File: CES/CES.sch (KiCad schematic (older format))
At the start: 4 parts, among them J101 Barrel_Jack

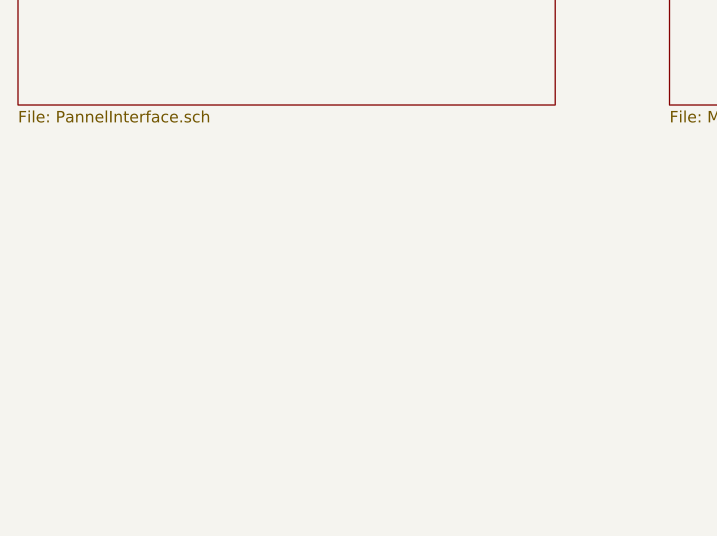
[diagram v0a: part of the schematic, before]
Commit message: Address decoding. Clock. Pannel buttons
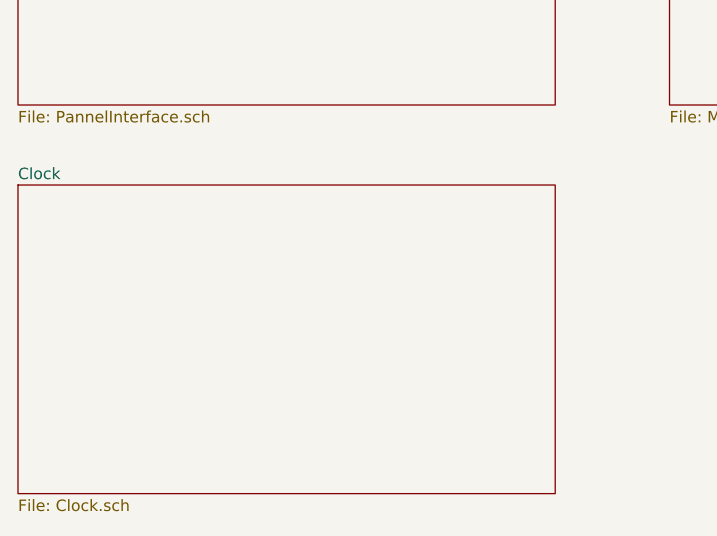
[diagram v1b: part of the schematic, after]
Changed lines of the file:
@@
 $Descr A4 11693 8268
 encoding utf-8
-Sheet 1 13
+Sheet 1 15
 Title "CES"
 Date "2021-04-24"
@@
 	10750 2200 10750 2150
 Connection ~ 10350 2200
+$Sheet
+S 1200 6000 2350 1350
+U 611BF25E
+F0 "Clock" 50
+F1 "Clock.sch" 50
+$EndSheet
 $EndSCHEMATC

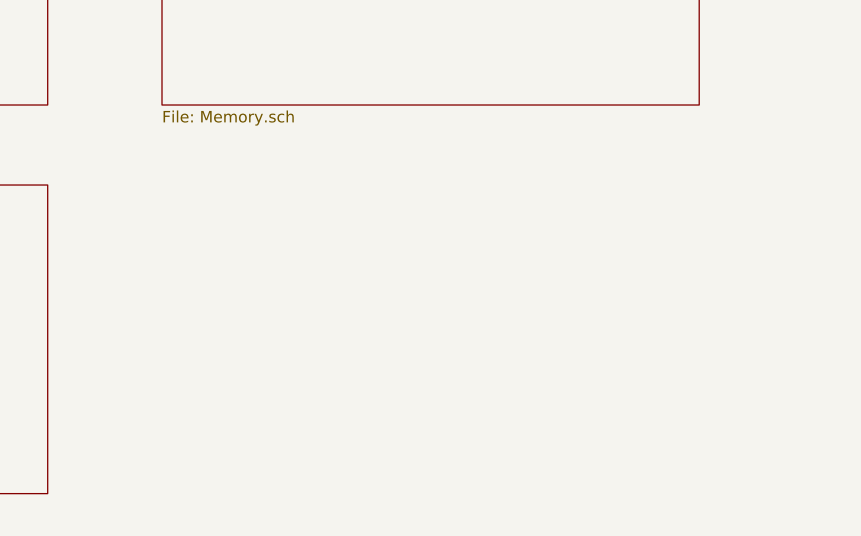
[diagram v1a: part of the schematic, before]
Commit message: ExpansionConnectors
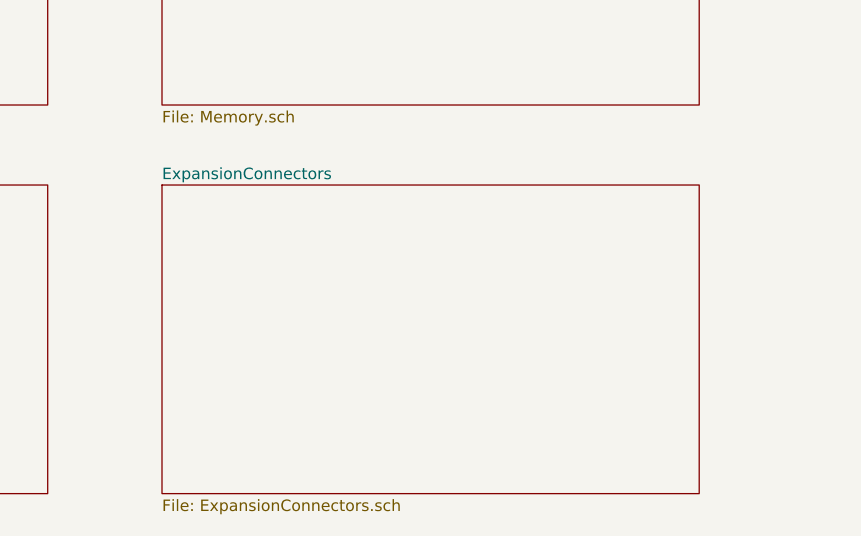
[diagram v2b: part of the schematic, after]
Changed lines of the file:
@@
 $Descr A4 11693 8268
 encoding utf-8
-Sheet 1 15
+Sheet 1 16
 Title "CES"
 Date "2021-04-24"
@@
 F1 "Clock.sch" 50
 $EndSheet
+$Sheet
+S 4050 6000 2350 1350
+U 60958E9E
+F0 "ExpansionConnectors" 50
+F1 "ExpansionConnectors.sch" 50
+$EndSheet
 $EndSCHEMATC

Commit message: Control Unit
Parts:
- gave numbers to parts that had none: 3
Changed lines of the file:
@@
 $Descr A4 11693 8268
 encoding utf-8
-Sheet 1 16
+Sheet 1 17
 Title "CES"
 Date "2021-04-24"
@@
 $EndBitmap
 $Comp
-L Device:CP1 C?
+L Device:CP1 C101
 U 1 1 60A155E7
 P 9800 2000
-F 0 "C?" H 9915 2046 50  0000 L CNN
+F 0 "C101" H 9915 2046 50  0000 L CNN
 F 1 "100uF" H 9915 1955 50  0000 L CNN
 F 2 "" H 9800 2000 50  0001 C CNN
@@
 $EndComp
 $Comp
-L Device:CP1 C?
+L Device:CP1 C102
 U 1 1 60A157F1
 P 10350 2000
-F 0 "C?" H 10465 2046 50  0000 L CNN
+F 0 "C102" H 10465 2046 50  0000 L CNN
 F 1 "10uF" H 10465 1955 50  0000 L CNN
 F 2 "" H 10350 2000 50  0001 C CNN
@@
 	9450 1800 9450 1750
 $Comp
-L Device:C C?
+L Device:C C103
 U 1 1 60A17721
 P 10750 2000
-F 0 "C?" H 10865 2046 50  0000 L CNN
+F 0 "C103" H 10865 2046 50  0000 L CNN
 F 1 "1000nF" H 10865 1955 50  0000 L CNN
 F 2 "" H 10788 1850 50  0001 C CNN

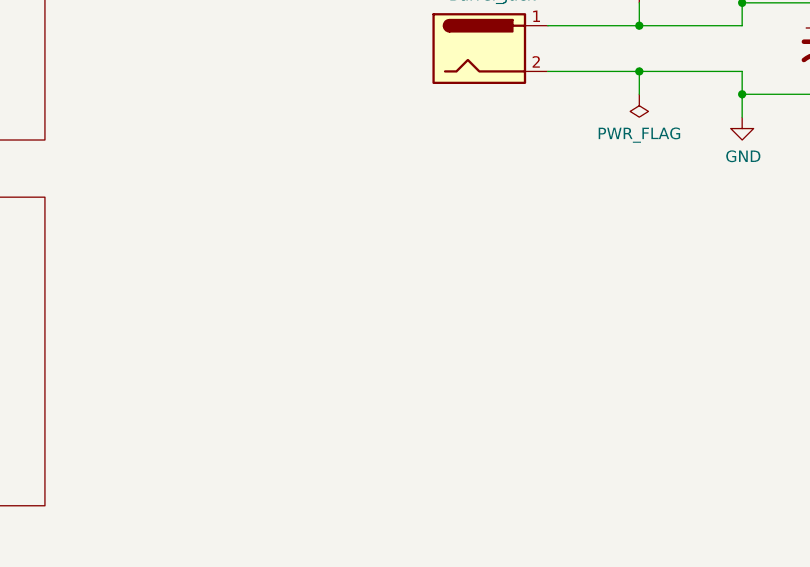
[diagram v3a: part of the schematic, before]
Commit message: Correcting ERC issues
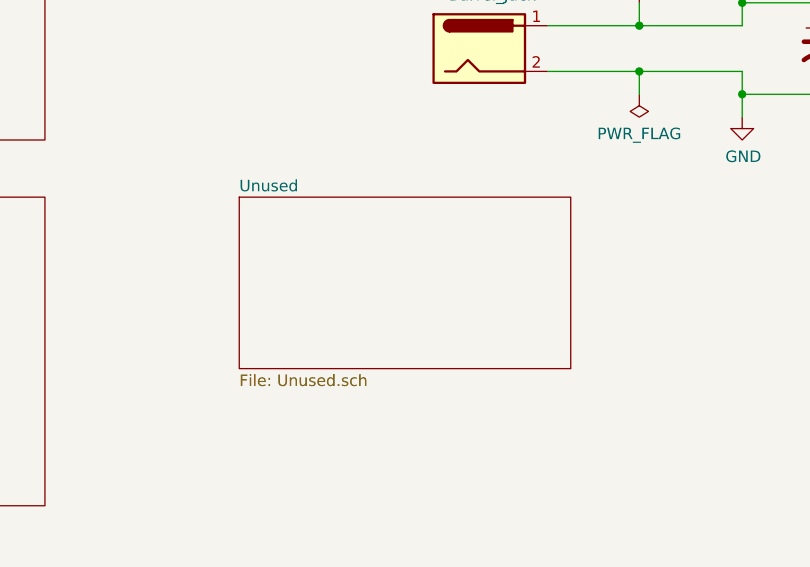
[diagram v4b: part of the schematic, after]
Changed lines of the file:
@@
 $Descr A4 11693 8268
 encoding utf-8
-Sheet 1 17
+Sheet 1 18
 Title "CES"
 Date "2021-04-24"
@@
 F1 "ExpansionConnectors.sch" 50
 $EndSheet
+$Sheet
+S 7250 2650 1450 750
+U 610111E8
+F0 "Unused" 50
+F1 "Unused.sch" 50
+$EndSheet
 $EndSCHEMATC

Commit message: Assigning footprints and generating netlist
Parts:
- C101, C102, C103: footprint (none) -> Capacitor_THT:CP_Radial_D5.0mm_P2.50mm
- J101: footprint (none) -> Connector_BarrelJack:BarrelJack_CUI_PJ-063AH_Horizontal
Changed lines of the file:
@@
 F 0 "J101" H 8357 2325 50  0000 C CNN
 F 1 "Barrel_Jack" H 8357 2234 50  0000 C CNN
-F 2 "" H 8350 1960 50  0001 C CNN
+F 2 "Connector_BarrelJack:BarrelJack_CUI_PJ-063AH_Horizontal" H 8350 1960 50  0001 C CNN
 F 3 "~" H 8350 1960 50  0001 C CNN
 	1    8300 2000
@@
 F 0 "C101" H 9915 2046 50  0000 L CNN
 F 1 "100uF" H 9915 1955 50  0000 L CNN
-F 2 "" H 9800 2000 50  0001 C CNN
+F 2 "Capacitor_THT:CP_Radial_D5.0mm_P2.50mm" H 9800 2000 50  0001 C CNN
 F 3 "~" H 9800 2000 50  0001 C CNN
 	1    9800 2000
@@
 F 0 "C102" H 10465 2046 50  0000 L CNN
 F 1 "10uF" H 10465 1955 50  0000 L CNN
-F 2 "" H 10350 2000 50  0001 C CNN
+F 2 "Capacitor_THT:CP_Radial_D5.0mm_P2.50mm" H 10350 2000 50  0001 C CNN
 F 3 "~" H 10350 2000 50  0001 C CNN
 	1    10350 2000
@@
 F 0 "C103" H 10865 2046 50  0000 L CNN
 F 1 "1000nF" H 10865 1955 50  0000 L CNN
-F 2 "" H 10788 1850 50  0001 C CNN
+F 2 "Capacitor_THT:CP_Radial_D5.0mm_P2.50mm" H 10788 1850 50  0001 C CNN
 F 3 "~" H 10750 2000 50  0001 C CNN
 	1    10750 2000
